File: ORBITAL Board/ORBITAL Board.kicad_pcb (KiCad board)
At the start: 4 copper layers, 94 x 94 mm, 108 parts, among them J1 Conn_01x02, J2 Micro_SD_Card_Det, J3 Conn_01x12, J4 Conn_01x12, P1 USB_C_Plug_USB2.0, U1 PTPS563206DRLR, U2 W25Q128JVS, U3 USBLC6-2SC6, U5 BNO085, U5 RP2040, U6 STSPIN220, U8 MS5607-02BA, Y1 ABLS-12.000MHZ-B4-T

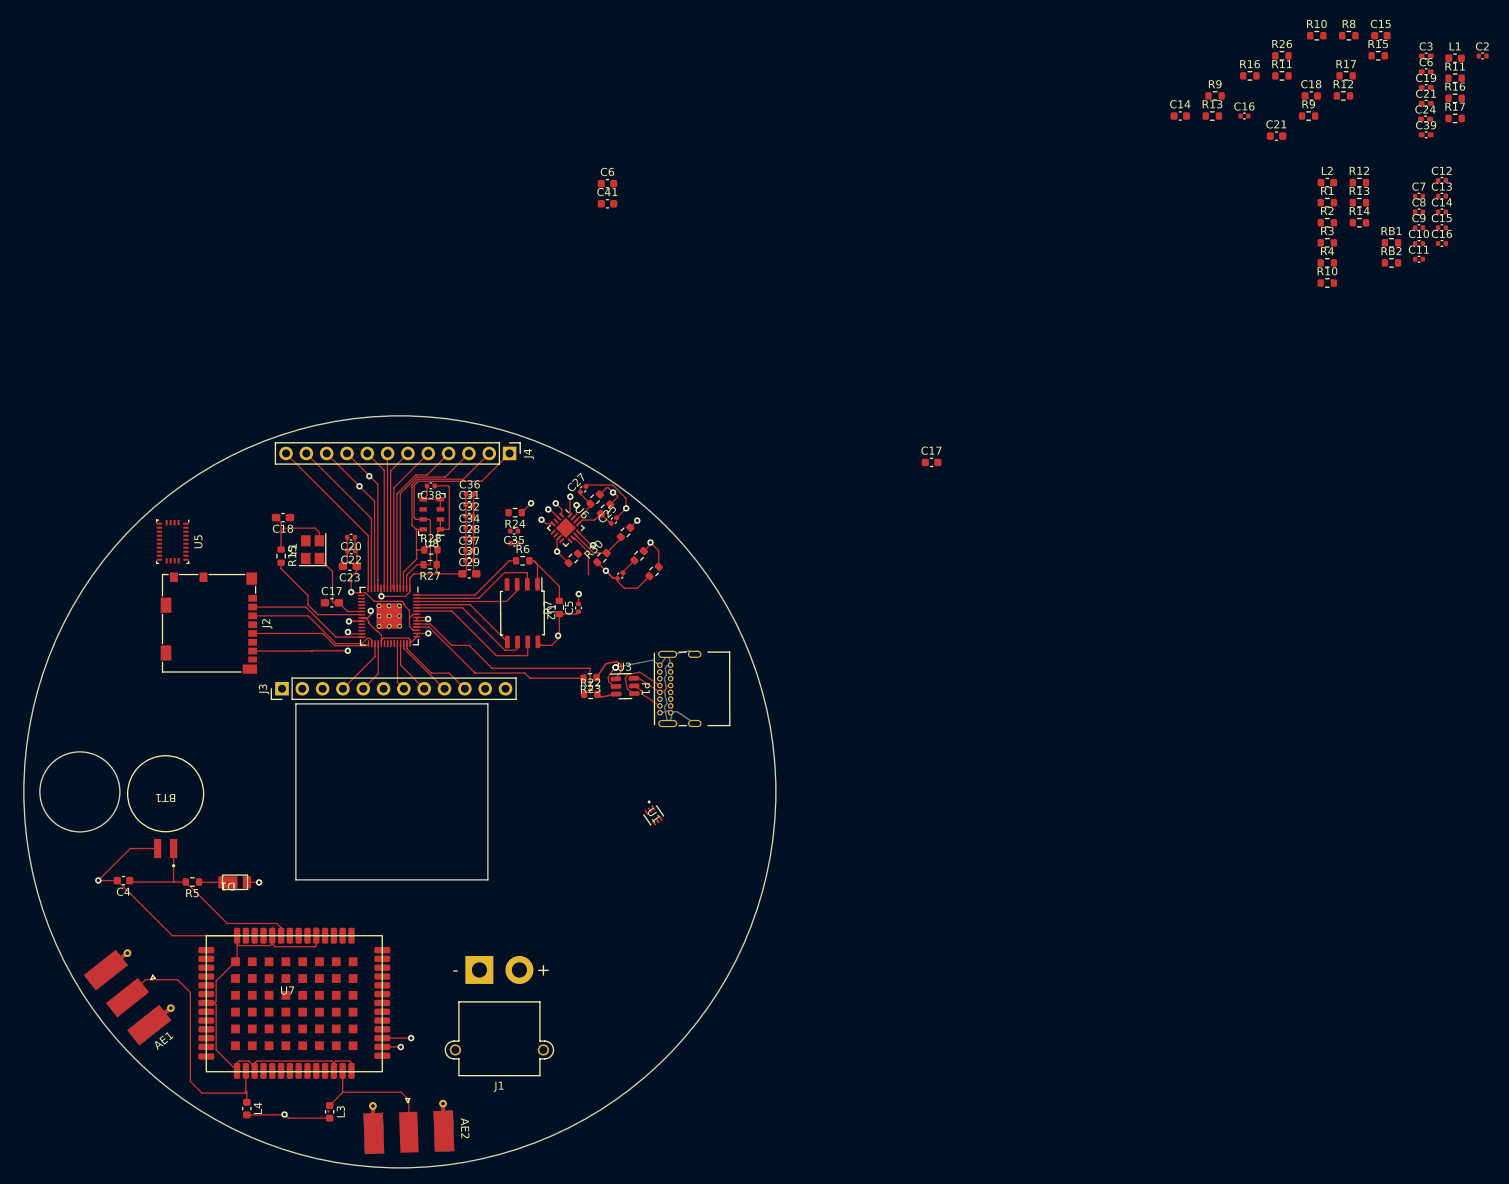
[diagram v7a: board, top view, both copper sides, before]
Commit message: Adding in LTC3118 to PCB
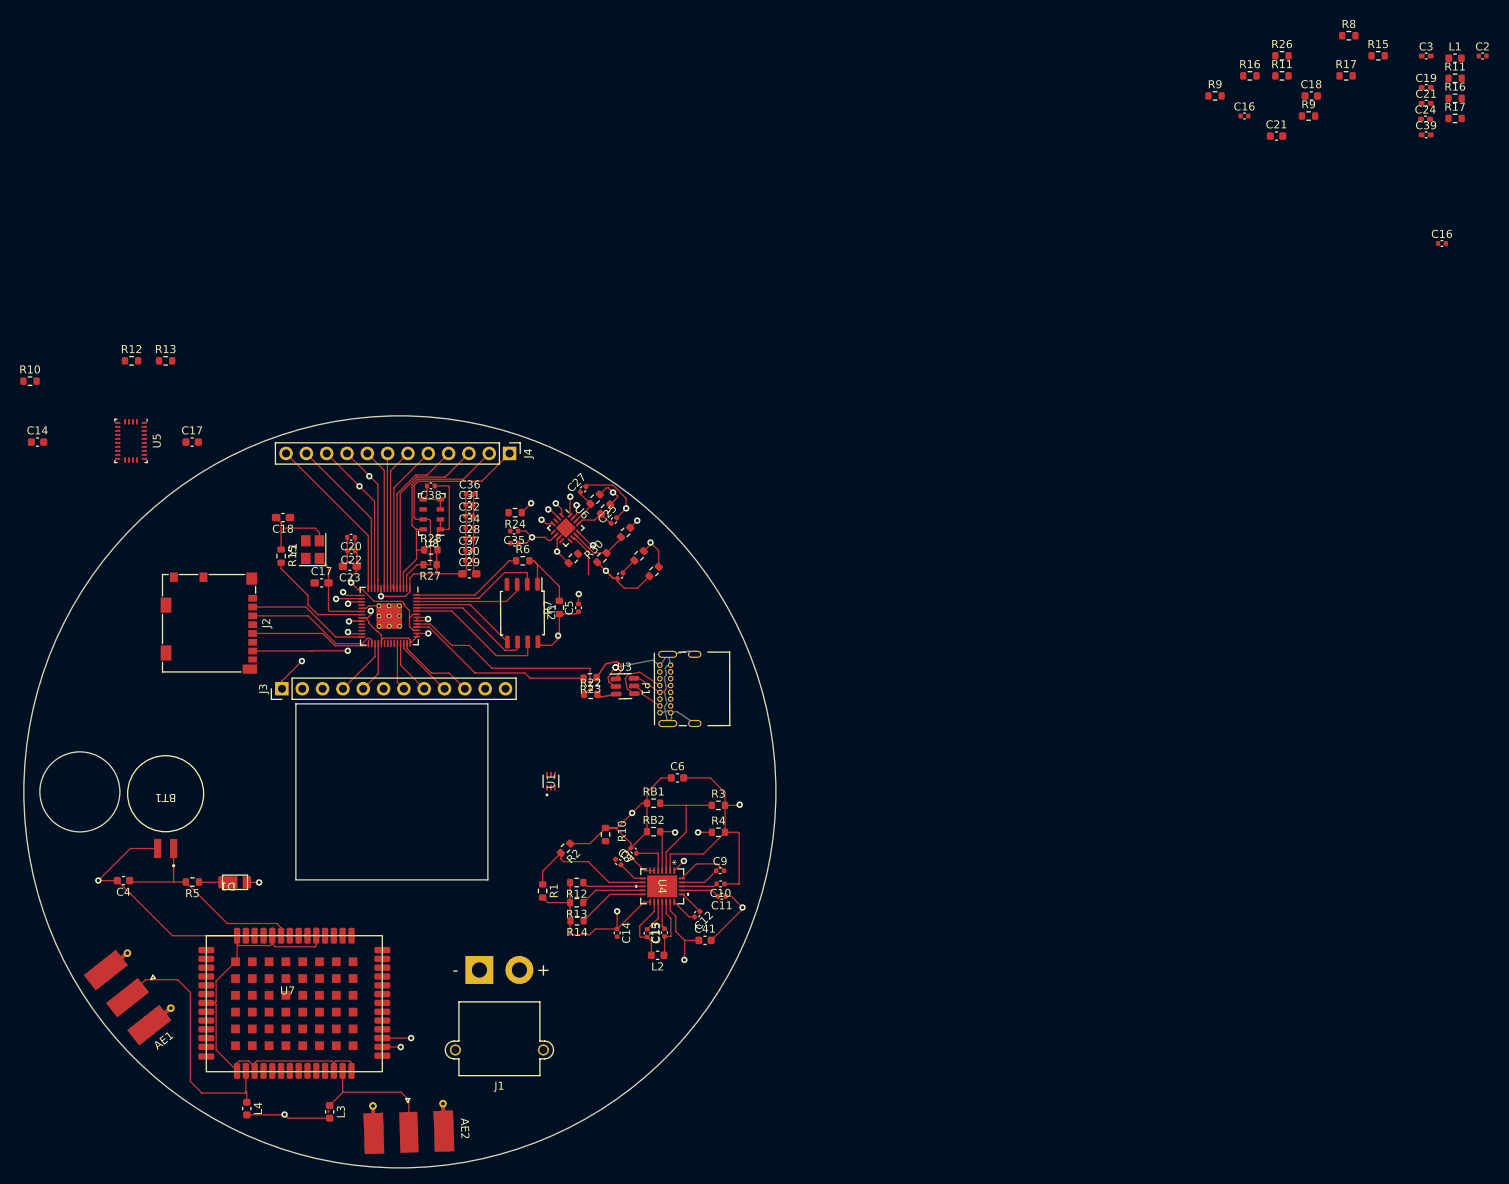
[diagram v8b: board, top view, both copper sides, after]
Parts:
- removed the C15 at (197.6, 30.5)
- removed the C6 at (203.3, 35.0)
- added U4: LTC3118, DCDC Converters:LTC3118, F.Cu at (107.8, 136.8)
- moved R10 166.5 mm to (28.8, 73.7)
- moved R12 155.1 mm to (41.5, 71.1)
- moved C14 148.5 mm to (29.7, 81.3)
- moved C14 136.9 mm to (102.2, 142.6), turned to -90 degrees
- moved R13 134.4 mm to (45.7, 71.1)
- moved C13 133.8 mm to (108.1, 142.6), turned to 90 degrees
- moved C15 132.8 mm to (105.9, 142.7), turned to -90 degrees
- moved R13 131.3 mm to (97.1, 138.8), turned to 180 degrees
- moved R12 131.3 mm to (97.1, 136.3), turned to 180 degrees
- moved R14 131.1 mm to (97.1, 141.1), turned to 180 degrees
- moved C12 130.7 mm to (112.2, 140.3), turned to -135 degrees
- moved R1 130.5 mm to (92.8, 137.4), turned to -90 degrees
- moved C8 128.9 mm to (102.3, 133.8), turned to -45 degrees
- moved L2 127.8 mm to (107.2, 145.4), turned to 180 degrees
- moved C7 127.8 mm to (104.2, 132.3), turned to 135 degrees
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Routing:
- net +6V: track 0.00 -> 83.5 mm, vias 0 -> 2
- net VBUS: track 12.2 -> 68.3 mm, vias 0 -> 1
- net GND: track 160.6 -> 206.4 mm, vias 7 -> 10
- net +BATT: track 0.00 -> 30.9 mm, vias 0 -> 1
- net /D12: track 0.00 -> 18.3 mm, vias 0 -> 2
- net Net-(U4-FB): track 0.00 -> 17.1 mm
- net /D13: track 0.00 -> 16.2 mm, vias 0 -> 1
- net Net-(U4-RUN1): track 0.00 -> 15.8 mm
- net /D14: track 0.86 -> 14.6 mm, vias 0 -> 1
- net Net-(U4-RUN2): track 0.00 -> 11.5 mm, vias 0 -> 2
- net Net-(U4-PGD): track 0.00 -> 8.73 mm
- net Net-(U4-SW2): track 0.00 -> 8.50 mm
- net Net-(U4-V2GD): track 0.00 -> 8.05 mm
- net Net-(U4-SW1): track 0.00 -> 7.73 mm
- net Net-(U4-V1GD): track 0.00 -> 7.61 mm
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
